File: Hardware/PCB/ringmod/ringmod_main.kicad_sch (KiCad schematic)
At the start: 63 parts, among them J1 Synth_power_2x5, U1 NE5532, U2 TL071, U3 TL072

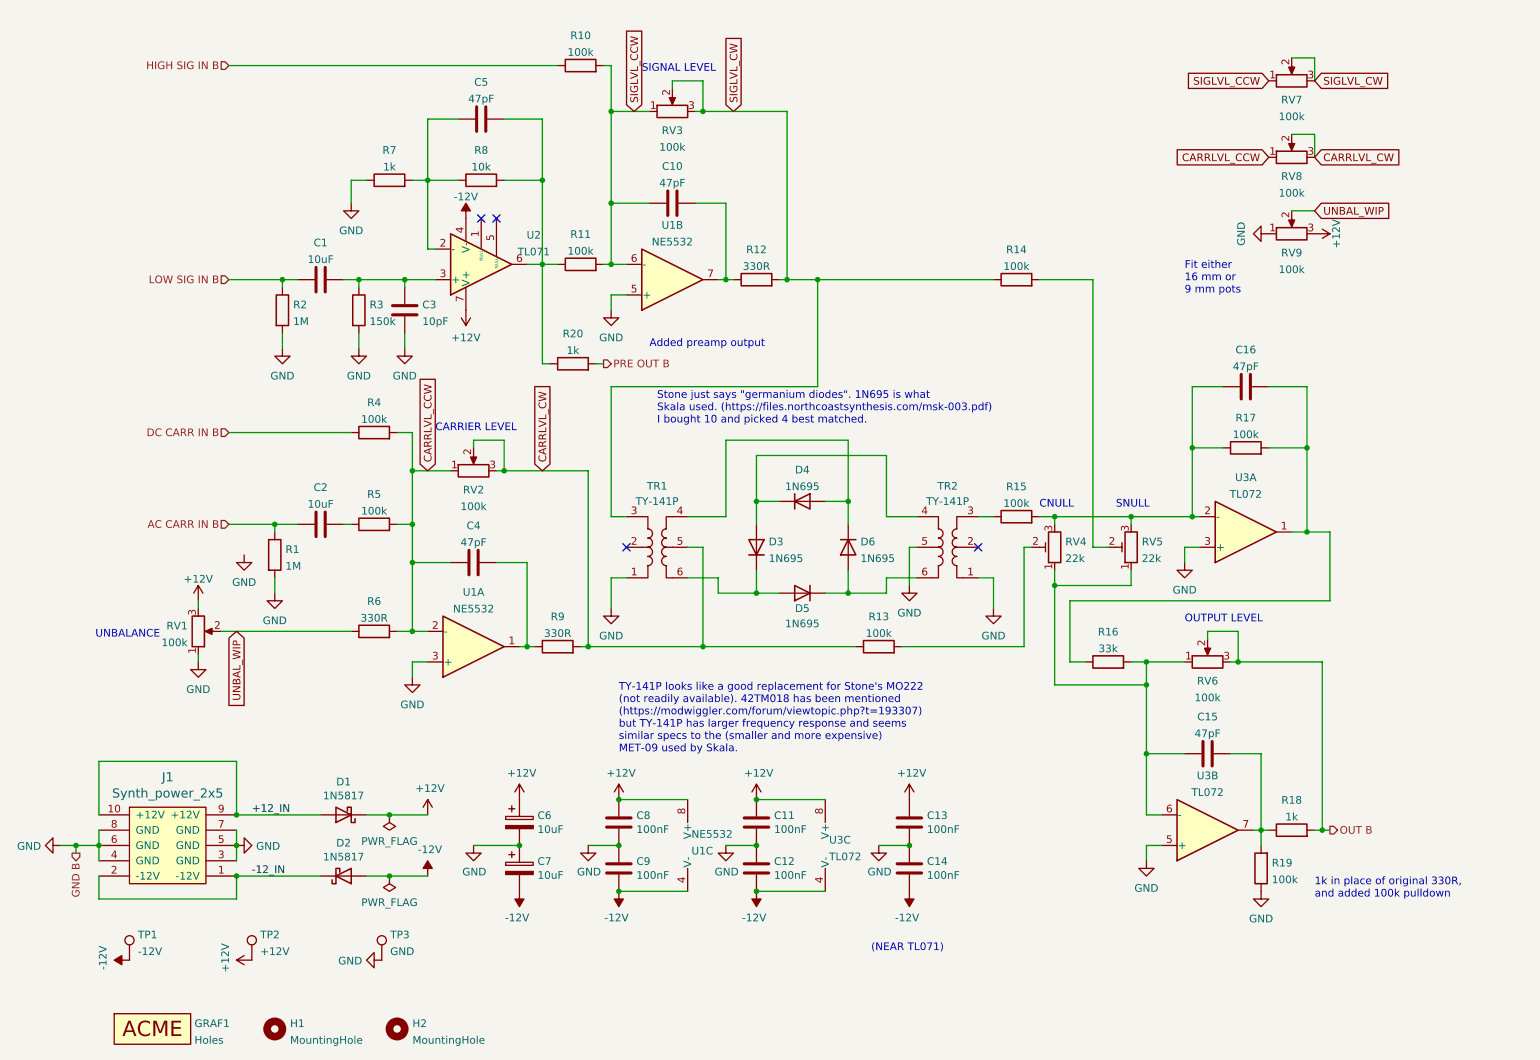
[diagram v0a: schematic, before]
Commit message: Update pot symbols
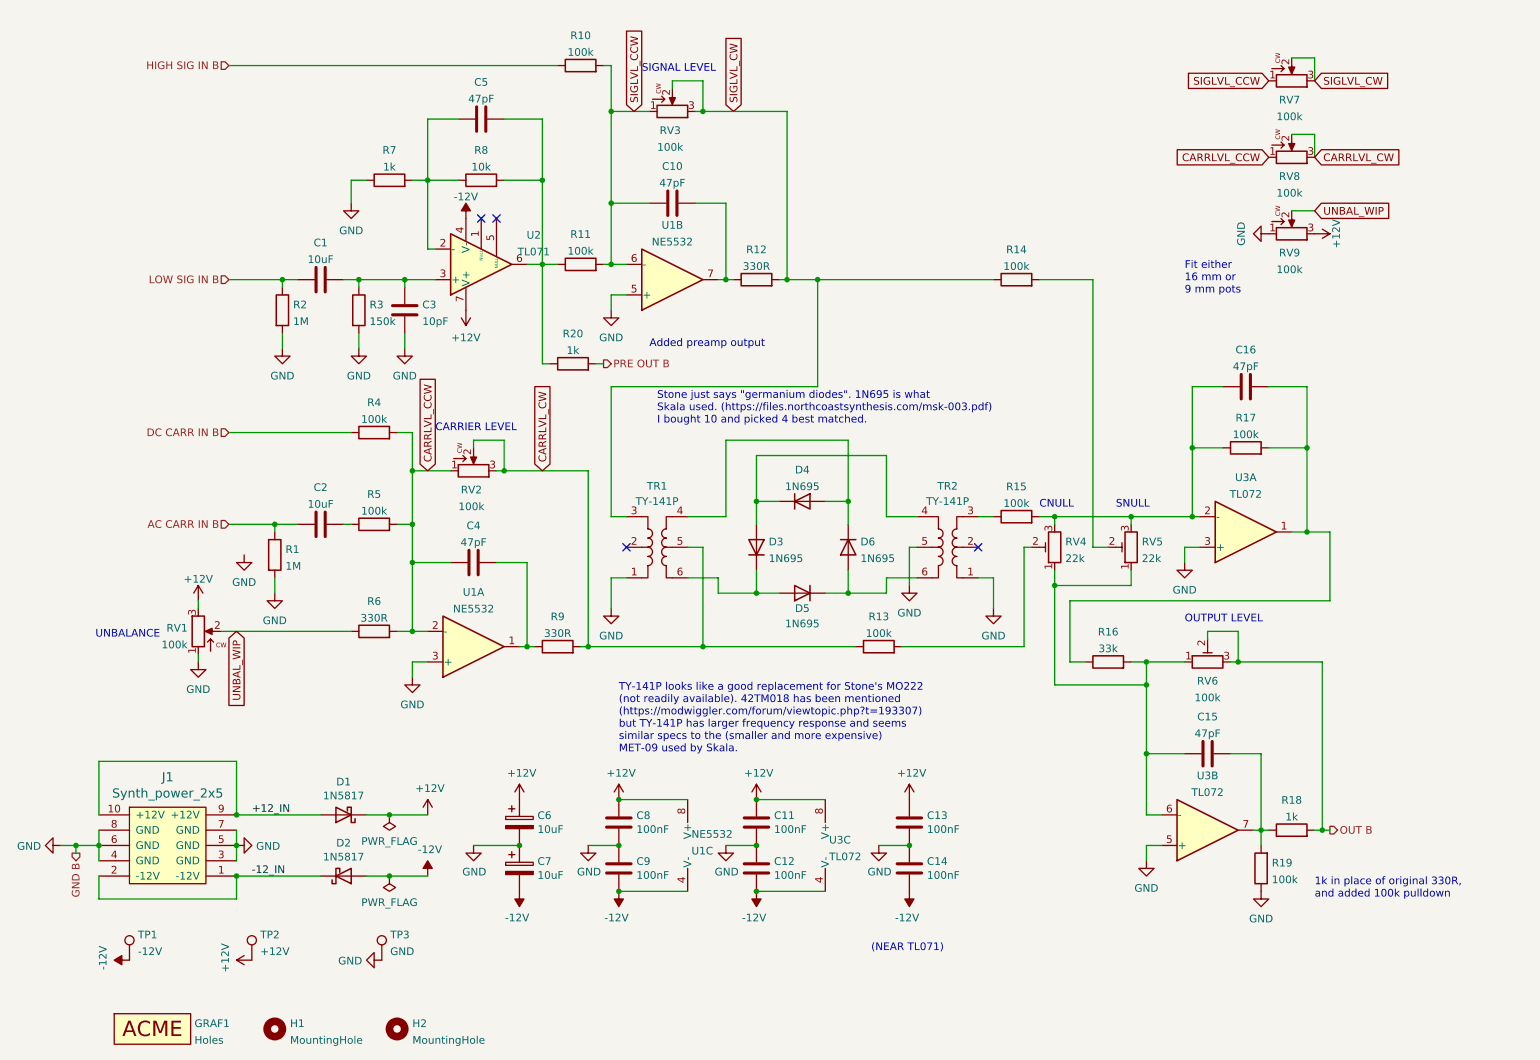
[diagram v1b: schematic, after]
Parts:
- RV6: symbol ao_symbols:R_POT -> ao_symbols:R_POT_TRIM_3296W
